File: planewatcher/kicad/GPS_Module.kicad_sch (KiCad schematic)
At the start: 9 parts, among them U1 LEA-M8T

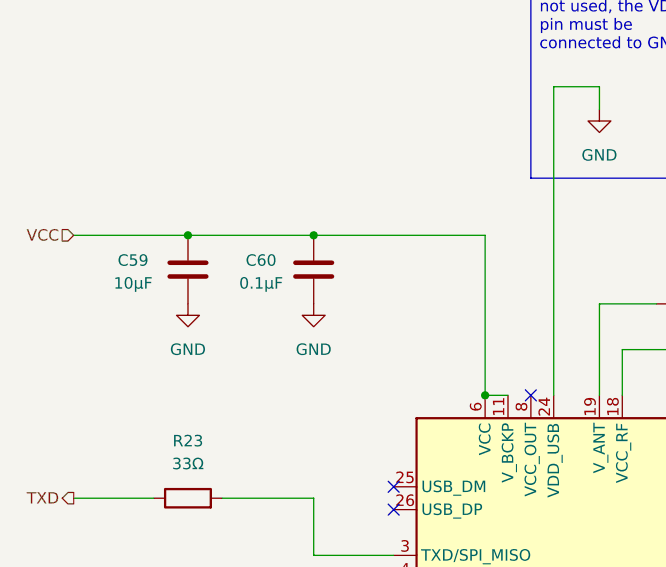
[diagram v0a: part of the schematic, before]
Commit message: review & consolidate all capacitors
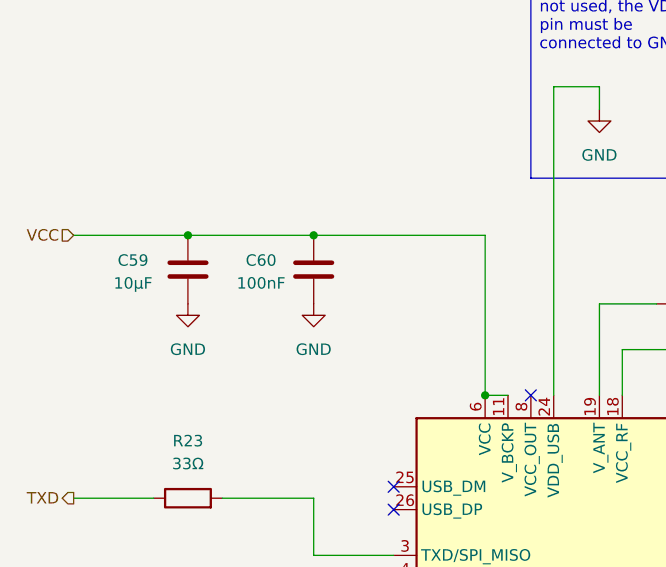
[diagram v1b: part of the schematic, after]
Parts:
- C59: MPN GRM188R61C106MA73D -> GRM188Z71A106MA73J; Manufacturer Murata -> Murata Electronics; Package 0603 -> 0603 (1608 Metric); Purpose Local bulk decoupling for the AD8138 analog supply. -> Local bulk decoupling for the GPS module.; Suggested Part Murata GRM188R61C106MA73D -> (none)
- C60: value 0.1µF -> 100nF; MPN GRM155R71H104KE14D -> GCM155R71A104KA55D; Manufacturer Murata -> Murata Electronics; Package 0402 -> 0402 (1005 Metric); Purpose Local high-frequency decoupling for the AD8138 analog suppl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 -> Local high-frequency decoupling for the GPS module.; Suggested Part Murata GRM155R71H104KE14D -> (none)
- C74: MPN GRM155R71H103KA88D -> GRM155R71C103KA01D; Manufacturer Murata -> Murata Electronics; Package 0402 -> 0402 (1005 Metric); Purpose ADL5513 VOUT/VSET measurement-mode support capacitor in the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 -> Filter cap for GPS module VCC_RF supply output pin.; Suggested Part Murata GRM155R71H103KA88D -> (none)
- D8: Suggested Part Infineon ESD101B102ELE6327XTMA1 -> (none)
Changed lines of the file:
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@@
 			)
 		)
-		(property "Datasheet" ""
+		(property "Datasheet" "https://search.murata.co.jp/Ceramy/image/img/A01X/G101/ENG/GRM188Z71A106MA73-01A.pdf"
 			(at 107.95 55.88 0)
 			(hide yes)
@@
 			)
 		)
-		(property "Description" "10µF, X5R, ±20%, 16V, 0603 MLCC"
+		(property "Description" "10 µF ±20% 10V Ceramic Capacitor X7R 0603 (1608 Metric)"
 			(at 107.95 55.88 0)
 			(hide yes)
@@
 			)
 		)
-		(property "Package" "0603"
+		(property "Package" "0603 (1608 Metric)"
 			(at 107.95 55.88 0)
 			(hide yes)
@@
 			)
 		)
-		(property "MPN" "GRM188R61C106MA73D"
+		(property "MPN" "GRM188Z71A106MA73J"
 			(at 107.95 55.88 0)
 			(hide yes)
@@
 			)
 		)
-		(property "Manufacturer" "Murata"
+		(property "Manufacturer" "Murata Electronics"
 			(at 107.95 55.88 0)
 			(hide yes)
@@
 			)
 		)
-		(property "Suggested Part" "Murata GRM188R61C106MA73D"
-			(at 107.95 55.88 0)
-			(hide yes)
-			(show_name no)
-			(do_not_autoplace no)
-			(effects
-				(font
-					(size 1.27 1.27)
-				)
-			)
-		)
-		(property "Purpose" "Local bulk decoupling for the AD8138 analog supply."
+		(property "Purpose" "Local bulk decoupling for the GPS module."
 			(at 107.95 55.88 0)
 			(hide yes)
@@
 		(property "Notes" ""
 			(at 107.95 55.88 90)
+			(hide yes)
+			(show_name no)
+			(do_not_autoplace no)
+			(effects
+				(font
+					(size 1.27 1.27)
+				)
+			)
+		)
+		(property "Mount_Type" ""
+			(at 107.95 55.88 0)
 			(hide yes)
 			(show_name no)
@@
 			)
 		)
-		(property "Suggested Part" "Infineon ESD101B102ELE6327XTMA1"
+		(property "Mount_Type" ""
 			(at 184.15 101.6 90)
 			(hide yes)
@@
 			)
 		)
+		(property "Mount_Type" ""
+			(at 163.83 59.69 90)
+			(hide yes)
+			(show_name no)
+			(do_not_autoplace no)
+			(effects
+				(font
+					(size 1.27 1.27)
+				)
+			)
+		)
 		(pin "1"
 		)
@@
 			)
 		)
-		(property "Datasheet" ""
+		(property "Datasheet" "https://search.murata.co.jp/Ceramy/image/img/A01X/G101/ENG/GRM155R71C103KA01-01.pdf"
 			(at 179.07 59.69 0)
 			(hide yes)
@@
 			)
 		)
-		(property "Description" "10nF, X7R, ±10%, 50V, 0402 MLCC"
+		(property "Description" "10000 pF ±10% 16V Ceramic Capacitor X7R 0402 (1005 Metric)"
 			(at 179.07 59.69 0)
 			(hide yes)
@@
 			)
 		)
-		(property "Package" "0402"
+		(property "Package" "0402 (1005 Metric)"
 			(at 179.07 59.69 0)
 			(hide yes)
@@
 			)
 		)
-		(property "MPN" "GRM155R71H103KA88D"
+		(property "MPN" "GRM155R71C103KA01D"
 			(at 179.07 59.69 0)
 			(hide yes)
@@
 			)
 		)
-		(property "Manufacturer" "Murata"
+		(property "Manufacturer" "Murata Electronics"
 			(at 179.07 59.69 0)
 			(hide yes)
@@
 			)
 		)
-		(property "Suggested Part" "Murata GRM155R71H103KA88D"
+		(property "Purpose" "Filter cap for GPS module VCC_RF supply output pin."
 			(at 179.07 59.69 0)
 			(hide yes)
@@
 			)
 		)
-		(property "Purpose" "ADL5513 VOUT/VSET measurement-mode support capacitor in the detector output network."
-			(at 179.07 59.69 0)
+		(property "Mount_Type" ""
+			(at 179.07 59.69 90)
 			(hide yes)
 			(show_name no)
@@
 			)
 		)
+		(property "Mount_Type" ""
+			(at 184.15 127 90)
+			(hide yes)
+			(show_name no)
+			(do_not_autoplace no)
+			(effects
+				(font
+					(size 1.27 1.27)
+				)
+			)
+		)
 		(pin "1"
 		)
@@
 			)
 		)
+		(property "Mount_Type" ""
+			(at 107.95 81.28 90)
+			(hide yes)
+			(show_name no)
+			(do_not_autoplace no)
+			(effects
+				(font
+					(size 1.27 1.27)
+				)
+			)
+		)
 		(pin "1"
 		)
@@
 			)
 		)
-		(property "Value" "0.1µF"
+		(property "Value" "100nF"
 			(at 116.078 57.404 0)
 			(show_name no)
@@
 			)
 		)
-		(property "Datasheet" ""
+		(property "Datasheet" "https://search.murata.co.jp/Ceramy/image/img/A01X/G101/ENG/GCM155R71A104KA55-01.pdf"
 			(at 121.92 55.88 0)
 			(hide yes)
@@
 			)
 		)
-		(property "Description" "100nF, X7R, ±10%, 50V, 0402 MLCC"
+		(property "Description" "0.1 µF ±10% 10V Ceramic Capacitor X7R 0402 (1005 Metric)"
 			(at 121.92 55.88 0)
 			(hide yes)
@@
 			)
 		)
-		(property "Package" "0402"
+		(property "Package" "0402 (1005 Metric)"
 			(at 121.92 55.88 0)
 			(hide yes)
@@
 			)
 		)
-		(property "MPN" "GRM155R71H104KE14D"
+		(property "MPN" "GCM155R71A104KA55D"
 			(at 121.92 55.88 0)
 			(hide yes)
@@
 			)
 		)
-		(property "Manufacturer" "Murata"
+		(property "Manufacturer" "Murata Electronics"
 			(at 121.92 55.88 0)
 			(hide yes)
@@
 			)
 		)
-		(property "Suggested Part" "Murata GRM155R71H104KE14D"
-			(at 121.92 55.88 0)
-			(hide yes)
-			(show_name no)
-			(do_not_autoplace no)
-			(effects
-				(font
-					(size 1.27 1.27)
-				)
-			)
-		)
-		(property "Purpose" "Local high-frequency decoupling for the AD8138 analog supply and VOCM network."
+		(property "Purpose" "Local high-frequency decoupling for the GPS module."
 			(at 121.92 55.88 0)
 			(hide yes)
@@
 		(property "Notes" ""
 			(at 121.92 55.88 90)
+			(hide yes)
+			(show_name no)
+			(do_not_autoplace no)
+			(effects
+				(font
+					(size 1.27 1.27)
+				)
+			)
+		)
+		(property "Mount_Type" ""
+			(at 121.92 55.88 0)
 			(hide yes)
 			(show_name no)
@@
 			)
 		)
+		(property "Mount_Type" ""
+			(at 148.59 95.25 0)
+			(hide yes)
+			(show_name no)
+			(do_not_autoplace no)
+			(effects
+				(font
+					(size 1.27 1.27)
+				)
+			)
+		)
 		(pin "3"
 		)
@@
 			(hide yes)
 			(show_name no)
+			(do_not_autoplace no)
+			(effects
+				(font
+					(size 1.27 1.27)
+				)
+			)
+		)
+		(property "Mount_Type" ""
+			(at 107.95 96.52 90)
+			(hide yes)
+			(show_name no)

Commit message: review & consolidate all resistors
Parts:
- R20: MPN (none) -> RE0402DRE0710RL; Manufacturer (none) -> YAGEO; Package (none) -> 0402 (1005 Metric); Purpose (none) -> Series resistor for GPS module V_ANT pin.
- R21, R23, R24: MPN (none) -> RC0402FR-0733RL; Manufacturer (none) -> YAGEO; Package (none) -> 0402 (1005 Metric); Purpose (none) -> Series damping/termination for GPS module digital I/O lines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
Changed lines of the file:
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@@
 			)
 		)
-		(property "Datasheet" ""
+		(property "Datasheet" "https://yageogroup.com/content/Resource%20Library/Datasheet/PYU-RE_105_ROHS_L.pdf"
 			(at 163.83 59.69 0)
 			(hide yes)
@@
 			)
 		)
-		(property "Description" "Resistor"
+		(property "Description" "10 Ohms ±0.5% 0.063W, 1/16W Chip Resistor 0402 (1005 Metric) Thick Film"
 			(at 163.83 59.69 0)
 			(hide yes)
@@
 		)
 		(property "Mount_Type" ""
+			(at 163.83 59.69 90)
+			(hide yes)
+			(show_name no)
+			(do_not_autoplace no)
+			(effects
+				(font
+					(size 1.27 1.27)
+				)
+			)
+		)
+		(property "MPN" "RE0402DRE0710RL"
+			(at 163.83 59.69 90)
+			(hide yes)
+			(show_name no)
+			(do_not_autoplace no)
+			(effects
+				(font
+					(size 1.27 1.27)
+				)
+			)
+		)
+		(property "Manufacturer" "YAGEO"
+			(at 163.83 59.69 90)
+			(hide yes)
+			(show_name no)
+			(do_not_autoplace no)
+			(effects
+				(font
+					(size 1.27 1.27)
+				)
+			)
+		)
+		(property "Package" "0402 (1005 Metric)"
+			(at 163.83 59.69 90)
+			(hide yes)
+			(show_name no)
+			(do_not_autoplace no)
+			(effects
+				(font
+					(size 1.27 1.27)
+				)
+			)
+		)
+		(property "Purpose" "Series resistor for GPS module V_ANT pin."
 			(at 163.83 59.69 90)
 			(hide yes)
@@
 			)
 		)
-		(property "Datasheet" ""
+		(property "Datasheet" "https://yageogroup.com/content/datasheet/asset/file/PYU-RC_GROUP_51_ROHS_L"
 			(at 184.15 127 0)
 			(hide yes)
@@
 			)
 		)
-		(property "Description" "Resistor"
+		(property "Description" "33 Ohms ±1% 0.063W, 1/16W Chip Resistor 0402 (1005 Metric) Moisture Resistant Thick Film"
 			(at 184.15 127 0)
 			(hide yes)
@@
 		)
 		(property "Mount_Type" ""
+			(at 184.15 127 90)
+			(hide yes)
+			(show_name no)
+			(do_not_autoplace no)
+			(effects
+				(font
+					(size 1.27 1.27)
+				)
+			)
+		)
+		(property "MPN" "RC0402FR-0733RL"
+			(at 184.15 127 90)
+			(hide yes)
+			(show_name no)
+			(do_not_autoplace no)
+			(effects
+				(font
+					(size 1.27 1.27)
+				)
+			)
+		)
+		(property "Manufacturer" "YAGEO"
+			(at 184.15 127 90)
+			(hide yes)
+			(show_name no)
+			(do_not_autoplace no)
+			(effects
+				(font
+					(size 1.27 1.27)
+				)
+			)
+		)
+		(property "Package" "0402 (1005 Metric)"
+			(at 184.15 127 90)
+			(hide yes)
+			(show_name no)
+			(do_not_autoplace no)
+			(effects
+				(font
+					(size 1.27 1.27)
+				)
+			)
+		)
+		(property "Purpose" "Series damping/termination for GPS module digital I/O lines into the FPGA header."
 			(at 184.15 127 90)
 			(hide yes)
@@
 			)
 		)
-		(property "Datasheet" ""
+		(property "Datasheet" "https://yageogroup.com/content/datasheet/asset/file/PYU-RC_GROUP_51_ROHS_L"
 			(at 107.95 81.28 0)
 			(hide yes)
@@
 			)
 		)
-		(property "Description" "Resistor"
+		(property "Description" "33 Ohms ±1% 0.063W, 1/16W Chip Resistor 0402 (1005 Metric) Moisture Resistant Thick Film"
 			(at 107.95 81.28 0)
 			(hide yes)
@@
 		)
 		(property "Mount_Type" ""
+			(at 107.95 81.28 90)
+			(hide yes)
+			(show_name no)
+			(do_not_autoplace no)
+			(effects
+				(font
+					(size 1.27 1.27)
+				)
+			)
+		)
+		(property "MPN" "RC0402FR-0733RL"
+			(at 107.95 81.28 90)
+			(hide yes)
+			(show_name no)
+			(do_not_autoplace no)
+			(effects
+				(font
+					(size 1.27 1.27)
+				)
+			)
+		)
+		(property "Manufacturer" "YAGEO"
+			(at 107.95 81.28 90)
+			(hide yes)
+			(show_name no)
+			(do_not_autoplace no)
+			(effects
+				(font
+					(size 1.27 1.27)
+				)
+			)
+		)
+		(property "Package" "0402 (1005 Metric)"
+			(at 107.95 81.28 90)
+			(hide yes)
+			(show_name no)
+			(do_not_autoplace no)
+			(effects
+				(font
+					(size 1.27 1.27)
+				)
+			)
+		)
+		(property "Purpose" "Series damping/termination for GPS module digital I/O lines into the FPGA header."
 			(at 107.95 81.28 90)
 			(hide yes)
@@
 			)
 		)
-		(property "Datasheet" ""
+		(property "Datasheet" "https://yageogroup.com/content/datasheet/asset/file/PYU-RC_GROUP_51_ROHS_L"
 			(at 107.95 96.52 0)
 			(hide yes)
@@
 			)
 		)
-		(property "Description" "Resistor"
+		(property "Description" "33 Ohms ±1% 0.063W, 1/16W Chip Resistor 0402 (1005 Metric) Moisture Resistant Thick Film"
 			(at 107.95 96.52 0)
 			(hide yes)
@@
 			(at 107.95 96.52 90)
 			(hide yes)
+			(show_name no)
+			(do_not_autoplace no)
+			(effects
+				(font
+					(size 1.27 1.27)
+				)
+			)
+		)
+		(property "MPN" "RC0402FR-0733RL"
+			(at 107.95 96.52 90)
+			(hide yes)
+			(show_name no)
+			(do_not_autoplace no)
+			(effects
+				(font
+					(size 1.27 1.27)
+				)
+			)
+		)
+		(property "Manufacturer" "YAGEO"
+			(at 107.95 96.52 90)
+			(hide yes)
+			(show_name no)
+			(do_not_autoplace no)
+			(effects
+				(font
+					(size 1.27 1.27)
+				)
+			)
+		)
+		(property "Package" "0402 (1005 Metric)"
+			(at 107.95 96.52 90)
+			(hide yes)
+			(show_name no)
+			(do_not_autoplace no)
+			(effects
+				(font
+					(size 1.27 1.27)
+				)
+			)
+		)
+		(property "Purpose" "Series damping/termination for GPS module digital I/O lines into the FPGA header."
+			(at 107.95 96.52 90)
+			(hide yes)

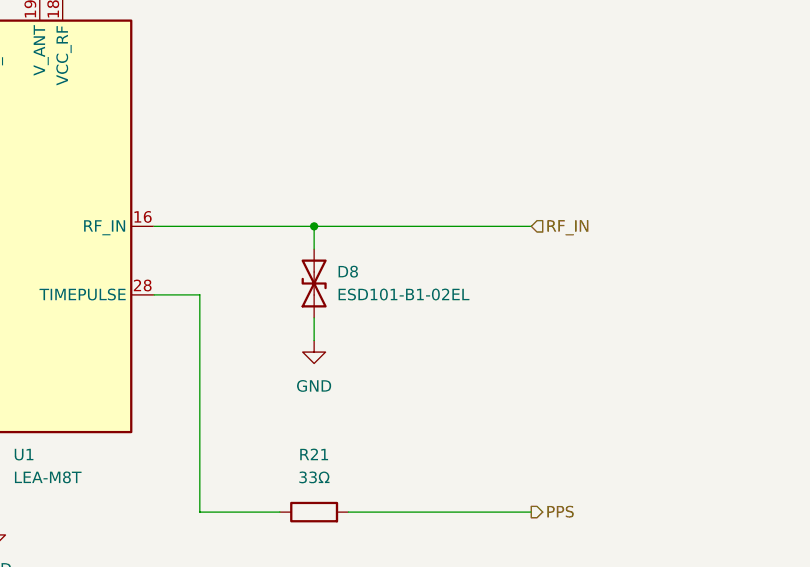
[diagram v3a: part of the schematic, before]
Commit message: swap TVS diodes with easier to source part
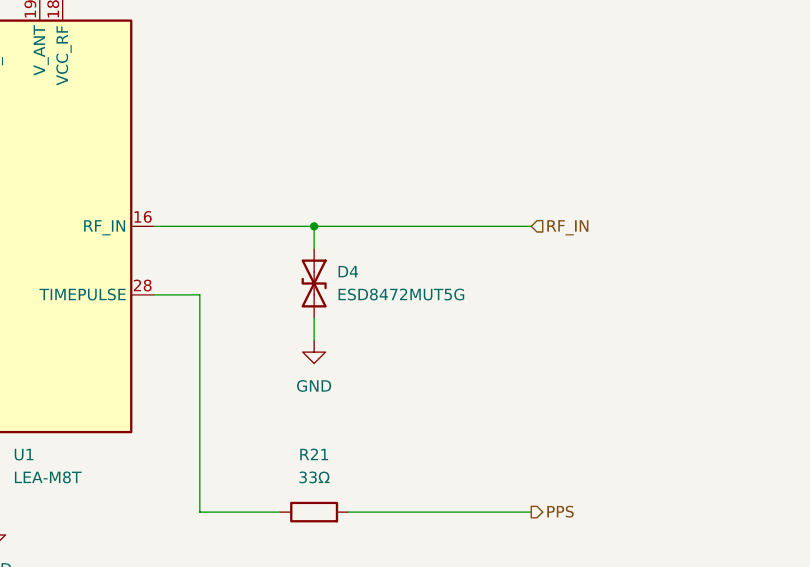
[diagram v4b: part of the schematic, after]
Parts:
- removed D8: ESD101-B1-02EL, planewatcher:D_ESD112-B1-02EL_TSLP-2-20, symbol Device:D_TVS
- added D4: ESD8472MUT5G, Diode_SMD:D_0201_0603Metric, symbol Device:D_TVS
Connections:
- net GND: now also D4.2 (A2)
- net RF_IN: now also D4.1 (A1)
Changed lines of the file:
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@@
-	)
-	(symbol
-		(lib_id "Device:D_TVS")
-		(at 184.15 101.6 90)
-		(unit 1)
-		(body_style 1)
-		(exclude_from_sim no)
-		(in_bom yes)
-		(on_board yes)
-		(in_pos_files yes)
-		(dnp no)
-		(fields_autoplaced yes)
-		(property "Reference" "D8"
-			(at 186.69 100.3299 90)
-			(show_name no)
-			(do_not_autoplace no)
-			(effects
-				(font
-					(size 1.27 1.27)
-				)
-				(justify right)
-			)
-		)
-		(property "Value" "ESD101-B1-02EL"
-			(at 186.69 102.8699 90)
-			(show_name no)
-			(do_not_autoplace no)
-			(effects
-				(font
-					(size 1.27 1.27)
-				)
-				(justify right)
-			)
-		)
-		(property "Footprint" "planewatcher:D_ESD112-B1-02EL_TSLP-2-20"
-			(at 184.15 101.6 0)
-			(hide yes)
-			(show_name no)
-			(do_not_autoplace no)
-			(effects
-				(font
-					(size 1.27 1.27)
-				)
-			)
-		)
-		(property "Datasheet" "https://www.infineon.com/assets/row/public/documents/24/49/infineon-esd101-b1-datasheet-en.pdf"
-			(at 184.15 101.6 0)
-			(hide yes)
-			(show_name no)
-			(do_not_autoplace no)
-			(effects
-				(font
-					(size 1.27 1.27)
-				)
-			)
-		)
-		(property "Description" "TVS (transient voltage suppressor) Bi-directional, 5.5 V, 0.1 pF, 0201, 0402, RoHS and halogen free compliant"
-			(at 184.15 101.6 0)
-			(hide yes)
-			(show_name no)
-			(do_not_autoplace no)
-			(effects
-				(font
-					(size 1.27 1.27)
-				)
-			)
-		)
-		(property "Package" "PG-TSLP-2-20"
-			(at 184.15 101.6 90)
-			(hide yes)
-			(show_name no)
-			(do_not_autoplace no)
-			(effects
-				(font
-					(size 1.27 1.27)
-				)
-			)
-		)
-		(property "MPN" "ESD101B102ELE6327XTMA1"
-			(at 184.15 101.6 90)
-			(hide yes)
-			(show_name no)
-			(do_not_autoplace no)
-			(effects
-				(font
-					(size 1.27 1.27)
-				)
-			)
-		)
-		(property "Manufacturer" "Infineon"
-			(at 184.15 101.6 90)
-			(hide yes)
-			(show_name no)
-			(do_not_autoplace no)
-			(effects
-				(font
-					(size 1.27 1.27)
-				)
-			)
-		)
-		(property "Purpose" "Provides low-capacitance ESD protection to chassis/board ground."
-			(at 184.15 101.6 90)
-			(hide yes)
-			(show_name no)
-			(do_not_autoplace no)
-			(effects
-				(font
-					(size 1.27 1.27)
-				)
-			)
-		)
-		(pin "1"
-		)
-		(pin "2"
-		)
-		(instances
-			(project "planewatcher"
-				(path "/7a4a4324-e8b8-4d06-b75a-28095d4e9f10/84812100-48e5-47cc-a358-d48bbae76aaf"
-					(reference "D8")
-					(unit 1)
-				)
-			)
-		)
 	)
 	(symbol
@@
 					(unit 1)
 				)
+			)
+		)
+	)
+	(symbol
+		(lib_id "Device:D_TVS")
+		(at 184.15 101.6 270)
+		(unit 1)
+		(body_style 1)
+		(exclude_from_sim no)
+		(in_bom yes)
+		(on_board yes)
+		(in_pos_files yes)
+		(dnp no)
+		(fields_autoplaced yes)
+		(property "Reference" "D4"
+			(at 186.69 100.3299 90)
+			(show_name no)
+			(do_not_autoplace no)
+			(effects
+				(font
+					(size 1.27 1.27)
+				)
+				(justify left)
+			)
+		)
+		(property "Value" "ESD8472MUT5G"
+			(at 186.69 102.8699 90)
+			(show_name no)
+			(do_not_autoplace no)
+			(effects
+				(font
+					(size 1.27 1.27)
+				)
+				(justify left)
+			)
+		)
+		(property "Footprint" "Diode_SMD:D_0201_0603Metric"
+			(at 184.15 101.6 0)
+			(hide yes)
+			(show_name no)
+			(do_not_autoplace no)
+			(effects
+				(font
+					(size 1.27 1.27)
+				)
+			)
+		)
+		(property "Datasheet" "https://www.onsemi.com/download/data-sheet/pdf/esd8472-d.pdf"
+			(at 184.15 101.6 0)
+			(hide yes)
+			(show_name no)
+			(do_not_autoplace no)
+			(effects
+				(font
+					(size 1.27 1.27)
+				)
+			)
+		)
+		(property "Description" "14V Clamp 3A (8/20µs) Ipp Tvs Diode Surface Mount 2-X3DFN (0.6x0.3) (0201)"
+			(at 184.15 101.6 0)
+			(hide yes)
+			(show_name no)
+			(do_not_autoplace no)
+			(effects
+				(font
+					(size 1.27 1.27)
+				)
+			)
+		)
+		(property "Package" "2-X3DFN (0.6x0.3) (0201)"
+			(at 184.15 101.6 0)
+			(hide yes)
+			(show_name no)
+			(do_not_autoplace no)
+			(effects
+				(font
+					(size 1.27 1.27)
+				)
+			)
+		)
+		(property "MPN" "ESD8472MUT5G"
+			(at 184.15 101.6 0)
+			(hide yes)
+			(show_name no)
+			(do_not_autoplace no)
+			(effects
+				(font
+					(size 1.27 1.27)
+				)
+			)
+		)
+		(property "Manufacturer" "onsemi"
+			(at 184.15 101.6 0)
+			(hide yes)
+			(show_name no)
+			(do_not_autoplace no)
+			(effects
+				(font
+					(size 1.27 1.27)
+				)
+			)
+		)
+		(property "Purpose" "Provides low-capacitance ESD protection to chassis/board ground for GPS RF input."
+			(at 184.15 101.6 90)
+			(hide yes)
+			(show_name no)
+			(do_not_autoplace no)
+			(effects
+				(font
+					(size 1.27 1.27)
+				)
+			)
+		)
+		(property "Notes" ""
+			(at 184.15 101.6 90)
+			(hide yes)
+			(show_name no)
+			(do_not_autoplace no)
+			(effects
+				(font
+					(size 1.27 1.27)
+				)
+			)
+		)
+		(pin "1"
+		)
+		(pin "2"
+		)
+		(instances
+			(project "planewatcher"
+				(path "/7a4a4324-e8b8-4d06-b75a-28095d4e9f10/84812100-48e5-47cc-a358-d48bbae76aaf"
+					(reference "D4")
+					(unit 1)
+				)

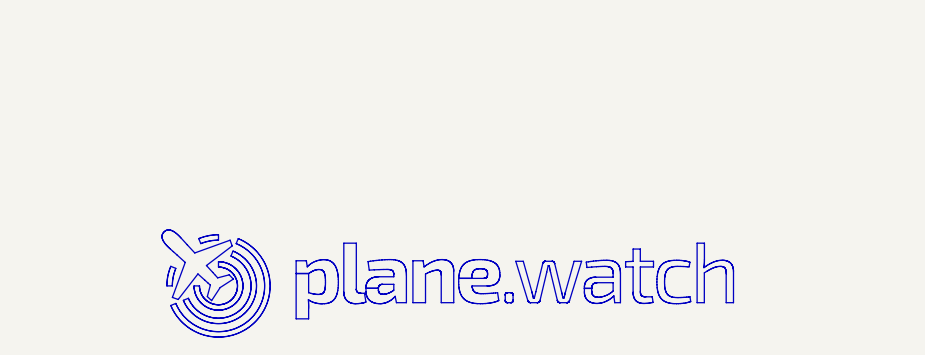
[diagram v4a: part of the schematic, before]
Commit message: add license & copyright info to schematic and pcb. fix layer window.
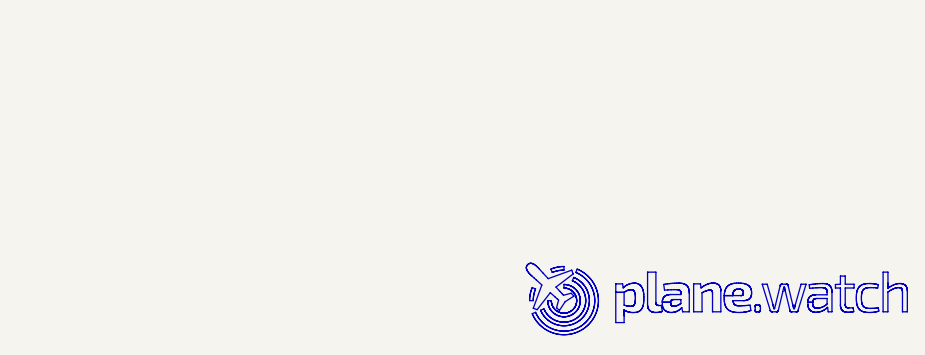
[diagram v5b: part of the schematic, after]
